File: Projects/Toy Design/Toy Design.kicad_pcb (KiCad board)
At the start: 2 copper layers, 170 x 120 mm, 85 parts, among them J1 Conn_01x01_Pin, J2 Conn_01x01_Pin, J3 FTSH-107-01-X-DV-K-TR, SW1 5GTH935, SW2 5GTH935, U1 TLV61048DBVR, U10 STM32G030K6T6, U11 MCP3208-CI/SL, U12 74HC595, U13 74HC595, U14 74HC595, U15 74HC595, U16 74HC595, U17 74HC595, U2 MCP73123, U3 NCP1117-5.0_SOT223, U4 MLX90333, U5 A1330, U6 A1330, U7 NCP1117-3.3_SOT223, U8 A1330, U9 TXU0104

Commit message: Cleaned up some traces
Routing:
- net OUT_U5: track 10.4 -> 179.9 mm
- net OUT_U6: track 7.54 -> 89.5 mm
- net OUT_U8: track 4.19 -> 64.0 mm
- net Net-(U10-PB1): track 4.73 -> 56.8 mm
- net NRST: track 2.52 -> 53.6 mm, vias 0 -> 2
- net SWDIO: track 0.00 -> 34.6 mm, vias 0 -> 1
- net SWCLK: track 0.00 -> 31.6 mm, vias 0 -> 1
- net MISO_SPI1: track 14.0 -> 42.5 mm
- net +3.3V: track 210.5 -> 233.9 mm
- net +5V: track 161.5 -> 158.0 mm
- net RCLK_LED: track 52.0 -> 48.7 mm
- net ~{OE}: track 115.0 -> 111.8 mm
- net GND: track 29.2 -> 31.6 mm
- net SPI2_SCK_LED: track 63.1 -> 61.3 mm

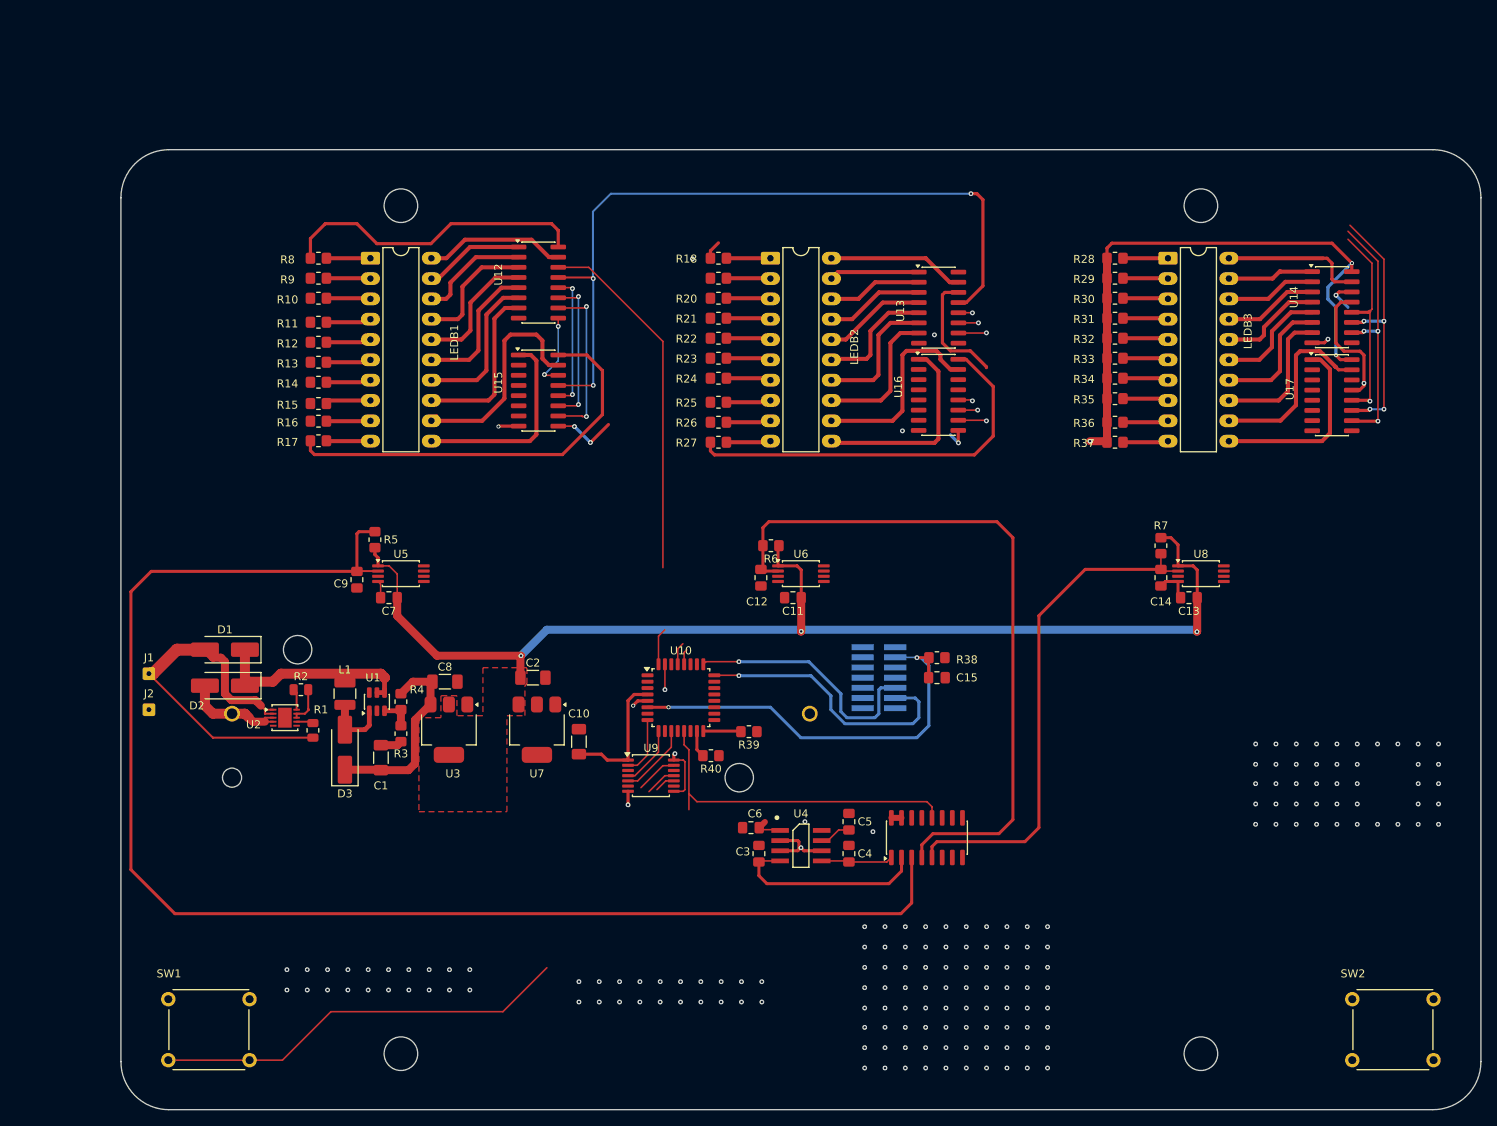
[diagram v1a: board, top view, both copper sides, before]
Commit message: Got more tracing done for clock pulses
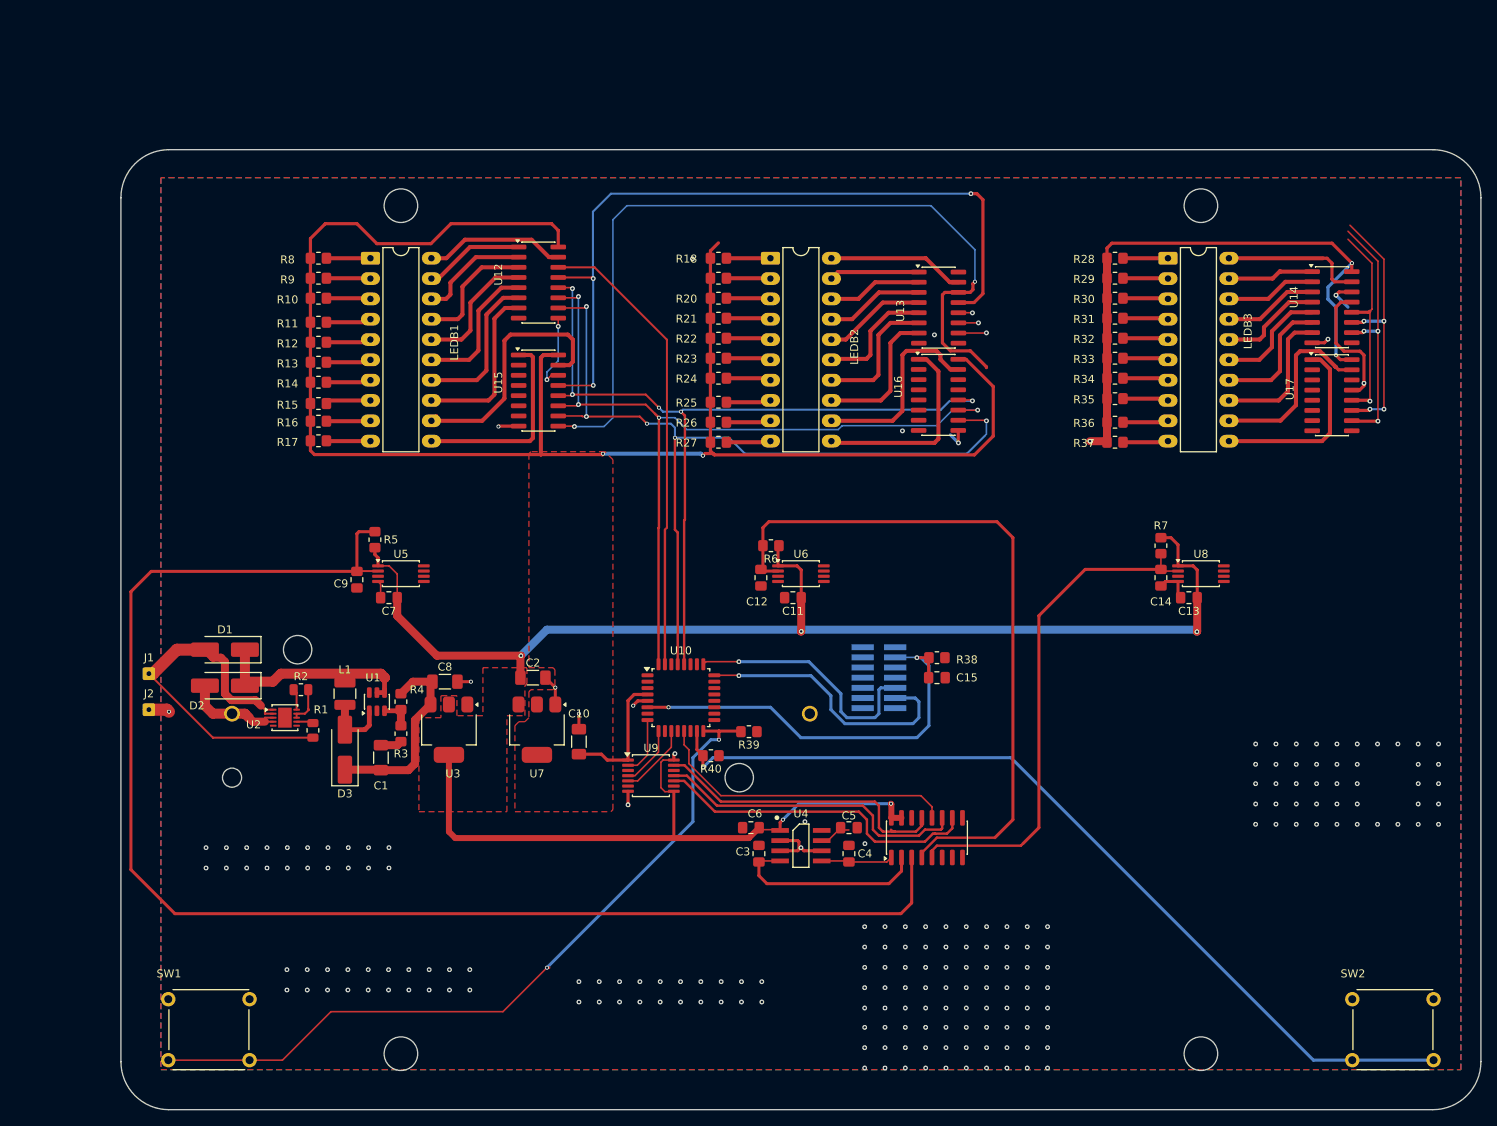
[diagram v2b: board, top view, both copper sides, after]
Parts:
- moved C5 0.75 mm to (187.5, 116.2), turned to 0 degrees
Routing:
- net Net-(U10-PB0): track 3.39 -> 112.4 mm, vias 0 -> 1
- net RCLK_LED: track 48.7 -> 130.0 mm, vias 5 -> 7
- net ~{SRCLR}: track 62.8 -> 143.7 mm, vias 7 -> 9
- net Net-(U13-SER): track 23.0 -> 102.3 mm
- net SPI2_SCK_LED: track 61.3 -> 139.7 mm, vias 8 -> 9
- net +5V: track 158.0 -> 230.1 mm
- net +3.3V: track 233.9 -> 294.5 mm, vias 4 -> 5
- net Net-(U10-PB1): track 56.8 -> 96.2 mm, vias 0 -> 2
- net Net-(U11-~{CS}/SHDN): track 2.57 -> 41.0 mm
- net Net-(U11-Din): track 3.94 -> 39.4 mm
- net Net-(U11-CLK): track 5.27 -> 38.0 mm
- net GND: track 31.6 -> 41.7 mm, vias 171 -> 198
- net SPI2_MOSI_LED: track 48.4 -> 58.0 mm, vias 1 -> 0
- net MISO_SPI1: track 42.5 -> 38.3 mm
- net Net-(U15-QA): track 28.3 -> 32.3 mm
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- added copper zone on F.Cu, net +3.3V
- added copper zone on B.Cu, net GND
- added copper zone on F.Cu, net GND

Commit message: Finalzied DRCs Added 3 LEDs
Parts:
- added C16: 10uF, Capacitor_SMD:C_1206_3216Metric_Pad1.33x1.80mm_HandSolder, F.Cu at (113.5, 90.2)
- added D4: LED, LED_THT:LED_D5.0mm, F.Cu at (165.2, 34.5)
- added D5: LED, LED_THT:LED_D5.0mm, F.Cu at (180.2, 34.5)
- added D6: LED, LED_THT:LED_D5.0mm, F.Cu at (195.2, 34.5)
- added R41: 650, Resistor_SMD:R_0805_2012Metric_Pad1.20x1.40mm_HandSolder, F.Cu at (85.1, 81.4)
- added R42: 650, Resistor_SMD:R_0805_2012Metric_Pad1.20x1.40mm_HandSolder, F.Cu at (172.4, 17.5)
- added R43: 650, Resistor_SMD:R_0805_2012Metric_Pad1.20x1.40mm_HandSolder, F.Cu at (172.4, 20.4)
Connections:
- U10 pad 1: unconnected-(U10-PB9-Pad1) -> ~{OE}
- U10 pad 14: unconnected-(U10-PA7-Pad14) -> Net-(U10-PA7)
- U10 pad 18: unconnected-(U10-PA8-Pad18) -> Net-(U10-PA8)
- U10 pad 22: unconnected-(U10-PA9/PA11-Pad22) -> Net-(U10-PA9/PA11)
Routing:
- net ~{OE}: track 112.3 -> 232.6 mm, vias 4 -> 5
- net +3.3V: track 294.5 -> 395.8 mm, vias 5 -> 7
- net Net-(U14-SER): track 7.24 -> 73.2 mm
- net RCLK_LED: track 130.0 -> 192.5 mm
- net SPI2_SCK_LED: track 139.7 -> 200.8 mm, vias 9 -> 10
- net ~{SRCLR}: track 143.7 -> 202.3 mm
- net Net-(U13-SER): track 102.3 -> 87.4 mm
- net GND: track 41.7 -> 55.4 mm, vias 198 -> 260
- net Net-(U14-QH'): track 0.00 -> 9.96 mm, vias 0 -> 2
- net Net-(U13-QH'): track 0.00 -> 8.24 mm, vias 0 -> 2
- net Net-(U13-QA): track 17.1 -> 21.5 mm
- net Net-(D1-K): track 26.2 -> 29.9 mm
- net Net-(U16-QA): track 25.0 -> 22.7 mm
- net Net-(U4-Vdig): track 3.95 -> 3.05 mm
- net +5V: track 230.1 -> 229.2 mm, vias 6 -> 5
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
